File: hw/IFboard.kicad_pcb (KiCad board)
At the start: 2 copper layers, 85 x 65.1 mm, 79 parts, among them J1 USB_C_Receptacle_USB2.0_16P, J2 Conn_01x03_Socket, J3 Conn_ARM_SWD_TagConnect_TC203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, J4 Conn_01x03_Socket, J5 Conn_01x03_Socket, J6 Conn_01x03_Socket, J7 Conn_01x01_MountingPin, SW3 SW_Push, SW4 SW_Push, SW5 SW_Push, SW6 SW_Push, U2 XC6206PxxxMR, U3 TCAN3413DR, U4 ST4E1240DT, U5 MAX232ESE+T, U6 STM32G0B1CBTx, U7 ER_OLEDM0.91_1x-I2C

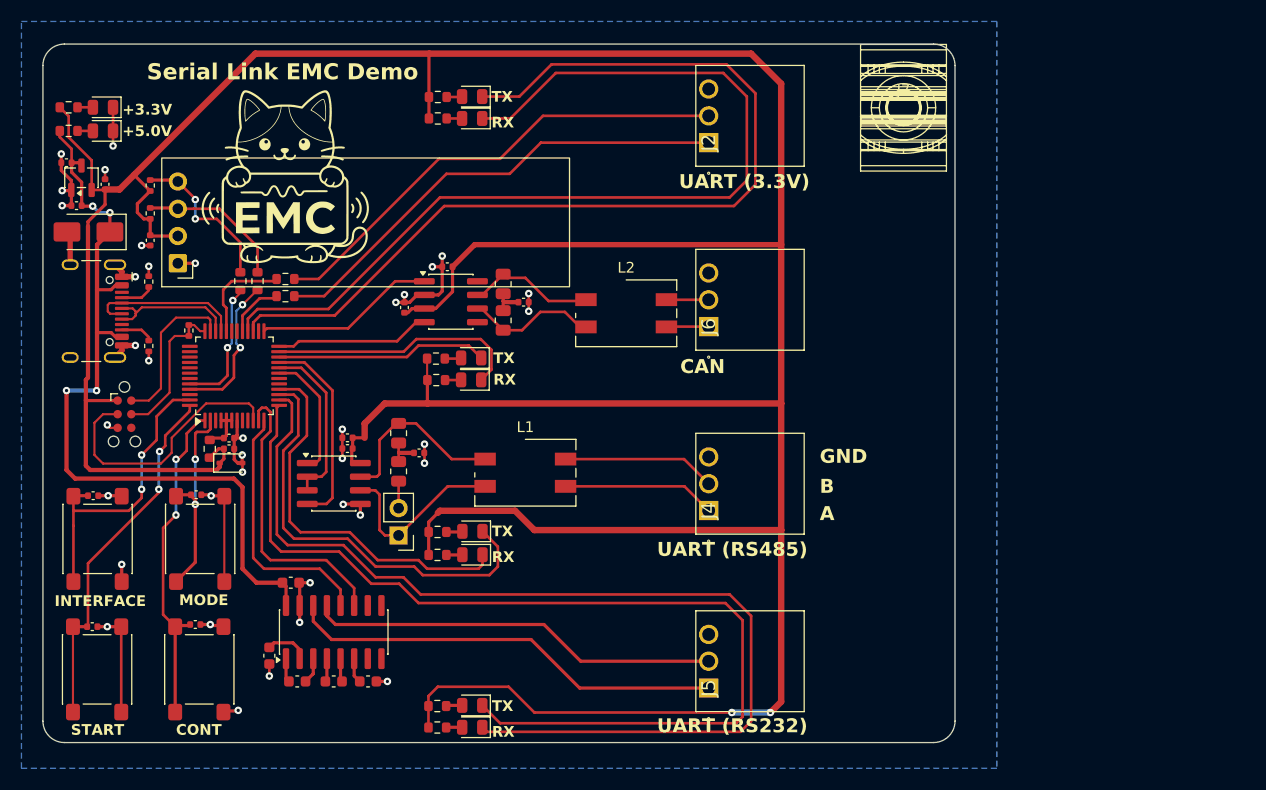
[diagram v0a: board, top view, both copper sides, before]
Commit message: changed position of SMSs and added TVS diodes to RS485 and CAN
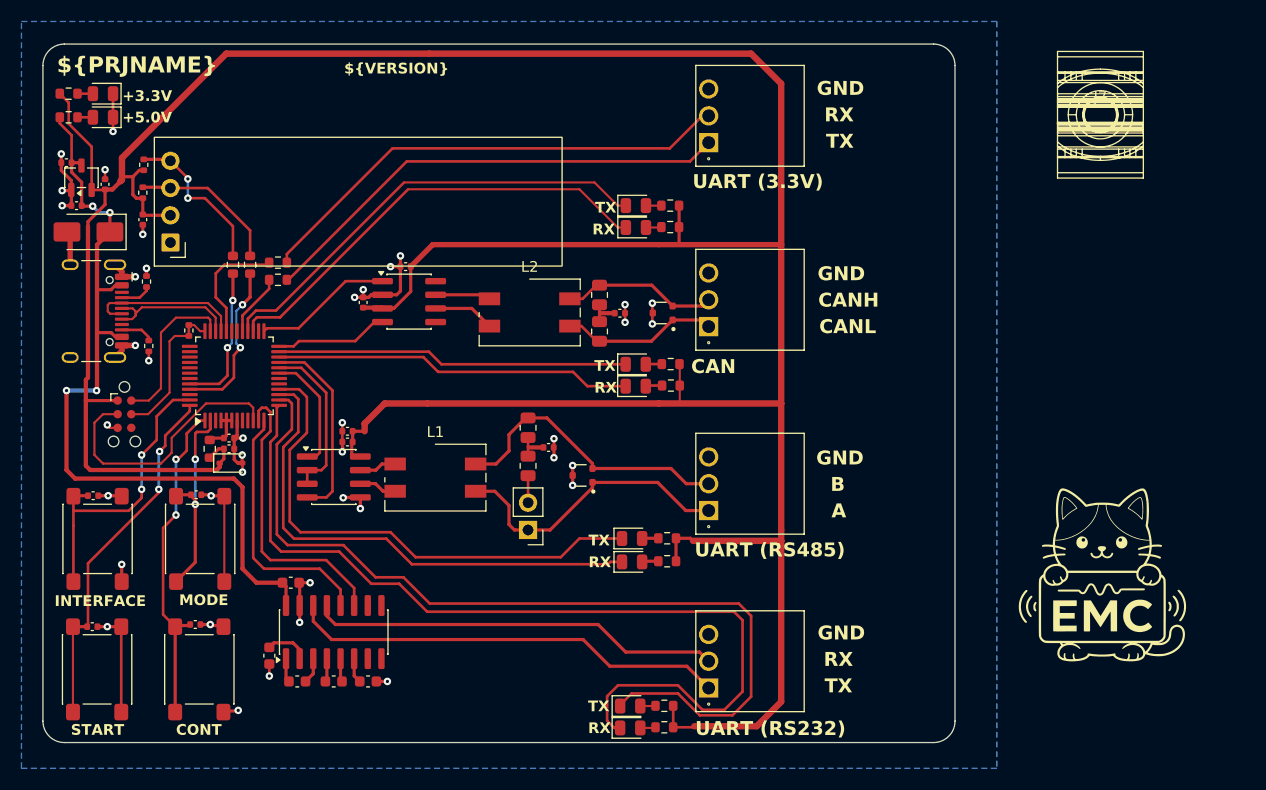
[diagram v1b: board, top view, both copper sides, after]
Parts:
- added D13: PESD2CANFD24V-UX, PZL:TVS_PESD2CANFD24V-UX, F.Cu at (108.7, 75.4)
- added D14: PESD2CANFD24V-UX, PZL:TVS_PESD2CANFD24V-UX, F.Cu at (101.2, 90.5)
- moved G*** 84.7 mm to (149.7, 99.7)
- moved R11 24.8 mm to (109.4, 67.4), turned to 0 degrees
- moved R10 23.1 mm to (109.4, 65.4), turned to 0 degrees
- moved R13 22.0 mm to (109.5, 82.2), turned to 0 degrees
- moved R12 21.9 mm to (109.4, 80.2), turned to 0 degrees
- moved R17 21.6 mm to (109.1, 98.5), turned to 0 degrees
- moved R16 21.5 mm to (109.1, 96.4), turned to 0 degrees
- moved R18 21.3 mm to (108.8, 112.0), turned to 0 degrees
- moved R19 21.2 mm to (108.8, 114.0), turned to 0 degrees
- moved D5 19.5 mm to (106.2, 67.4), turned to 0 degrees
- moved J7 18.4 mm to (149.5, 56.9)
- moved D4 17.3 mm to (106.2, 65.4), turned to 0 degrees
- moved D8 15.6 mm to (106.2, 82.2), turned to 0 degrees
- moved D6 15.4 mm to (106.2, 80.2), turned to 0 degrees
- moved D10 15.1 mm to (105.8, 98.6), turned to 0 degrees
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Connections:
- JP1 pad 1: Net-(JP1-A) -> Net-(J4-Pin_1)
- L1 pad 2: Net-(JP1-A) -> Net-(U4-A)
- R14 pad 1: Net-(U3-CANH) -> Net-(J6-Pin_2)
- R15 pad 2: Net-(U3-CANL) -> Net-(J6-Pin_1)
- R25 pad 2: Net-(U4-B) -> Net-(J4-Pin_2)
- U4 pad 6: Net-(JP1-A) -> Net-(U4-A)
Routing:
- net +3.3V: track 362.7 -> 315.0 mm, vias 2 -> 0
- net /USART1_RX_LED: track 89.3 -> 42.2 mm
- net /USART1_TX_LED: track 88.1 -> 42.5 mm
- net Net-(JP1-A): track 17.2 -> 0.00 mm
- net /CAN_RX_LED: track 19.8 -> 33.4 mm
- net /USART4_TX_LED: track 96.9 -> 83.3 mm
- net Net-(U4-B): track 16.9 -> 3.48 mm
- net Net-(J4-Pin_1): track 14.3 -> 27.5 mm
- net Net-(J4-Pin_2): track 14.3 -> 27.2 mm
- net /USART3_TX_LED: track 36.0 -> 48.0 mm
- net Net-(J6-Pin_2): track 3.94 -> 14.6 mm
- net Net-(J6-Pin_1): track 3.95 -> 14.6 mm
- net /USART4_RX_LED: track 94.2 -> 85.2 mm
- net /CAN_TX_LED: track 23.9 -> 32.8 mm
- net Net-(U3-CANH): track 12.0 -> 5.17 mm
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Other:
- board text added: "${PRJNAME}"
- board text added: "${VERSION}"
- board text added: "CANH"
- board text added: "CANL"
- board text removed: "Serial Link EMC Demo"

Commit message: wip:testpoints
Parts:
- added TP1: TestPoint, PZL:TestPoint_Keystone_5019_Miniature, F.Cu at (101.9, 70.6)
- added TP2: TestPoint, TestPoint:TestPoint_Keystone_5005-5009_Compact, F.Cu at (106.2, 72.8)
- added TP3: TestPoint, TestPoint:TestPoint_Keystone_5005-5009_Compact, F.Cu at (106.2, 78.0)
- added TP4: TestPoint, TestPoint:TestPoint_Keystone_5005-5009_Compact, F.Cu at (105.7, 87.6)
- added TP5: TestPoint, TestPoint:TestPoint_Keystone_5005-5009_Compact, F.Cu at (105.7, 93.1)
- moved D14 7.75 mm to (109.0, 90.5)
- moved D6 0.76 mm to (106.2, 80.9)
- moved D8 0.76 mm to (106.2, 83.0)
- moved R12 0.76 mm to (109.4, 80.9)
- moved R13 0.76 mm to (109.5, 82.9)
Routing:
- net +3.3V: track 315.0 -> 315.8 mm

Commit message: wip:testpoints
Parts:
- added JP2: Jumper_2_Open, Connector_PinHeader_2.54mm:PinHeader_1x02_P2.54mm_Vertical, F.Cu at (103.2, 68.9)
- added R26: 1k, Resistor_SMD:R_0603_1608Metric, F.Cu at (86.7, 77.8)
- added R27: 1k, Resistor_SMD:R_0603_1608Metric, F.Cu at (83.7, 77.8)
- added TP6: TestPoint, TestPoint:TestPoint_Keystone_5005-5009_Compact, F.Cu at (107.2, 58.3)
- added TP7: TestPoint, TestPoint:TestPoint_Keystone_5005-5009_Compact, F.Cu at (107.1, 53.4)
- added TP8: TestPoint, TestPoint:TestPoint_Keystone_5005-5009_Compact, F.Cu at (107.2, 108.3)
- added TP9: TestPoint, TestPoint:TestPoint_Keystone_5005-5009_Compact, F.Cu at (107.2, 104.0)
- U7: footprint Display:ER_OLEDM0.91_1x-I2C -> PZL:ER_OLEDM0.91_1x-I2C
- moved TP1 18.6 mm to (91.4, 55.2), turned to -90 degrees
- moved D5 4.10 mm to (105.9, 63.3)
- moved D4 4.10 mm to (105.9, 61.3)
- moved R10 4.10 mm to (109.1, 61.3)
- moved R11 4.10 mm to (109.1, 63.3)
- moved TP5 1.81 mm to (107.2, 94.0), turned to 90 degrees
- moved TP2 1.63 mm to (107.2, 71.5)
- moved TP4 1.61 mm to (107.2, 87.1)
- moved C20 1.61 mm to (104.2, 76.9)
- moved R15 1.61 mm to (102.3, 78.6)
- moved R14 1.44 mm to (102.2, 75.0)
- moved D10 1.27 mm to (105.8, 99.9)
- moved D9 1.27 mm to (105.8, 97.7)
- moved R16 1.27 mm to (109.1, 97.7)
- moved R17 1.27 mm to (109.1, 99.8)
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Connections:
- R14 pad 1: Net-(J6-Pin_2) -> Net-(JP2-B)
- U3 pad 5: unconnected-(U3-SHDN-Pad5) -> Net-(U3-SHDN)
- U3 pad 8: unconnected-(U3-S-Pad8) -> Net-(U3-S)
- U6 pad 26: unconnected-(U6-PB14-Pad26) -> /TODO_EN_CAN_TERM
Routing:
- net Net-(U3-S): track 0.00 -> 7.36 mm
- net Net-(J2-Pin_2): track 45.4 -> 49.7 mm
- net GND: track 87.7 -> 91.6 mm, vias 40 -> 43
- net Net-(J6-Pin_2): track 14.6 -> 18.4 mm
- net Net-(J2-Pin_1): track 44.5 -> 47.7 mm
- net Net-(JP2-B): track 0.00 -> 3.06 mm
- net Net-(J6-Pin_1): track 14.6 -> 17.5 mm
- net Net-(J4-Pin_1): track 27.0 -> 29.2 mm
- net Net-(J4-Pin_2): track 26.9 -> 29.0 mm
- net Net-(U3-SHDN): track 0.00 -> 1.61 mm
- net /USART1_RX_LED: track 42.2 -> 40.7 mm
- net Net-(U6-PB6): track 15.2 -> 13.9 mm
- net Net-(U6-PB5): track 13.5 -> 12.3 mm
- net /USART1_RX: track 11.4 -> 10.1 mm
- net /SCL: track 14.0 -> 15.3 mm
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
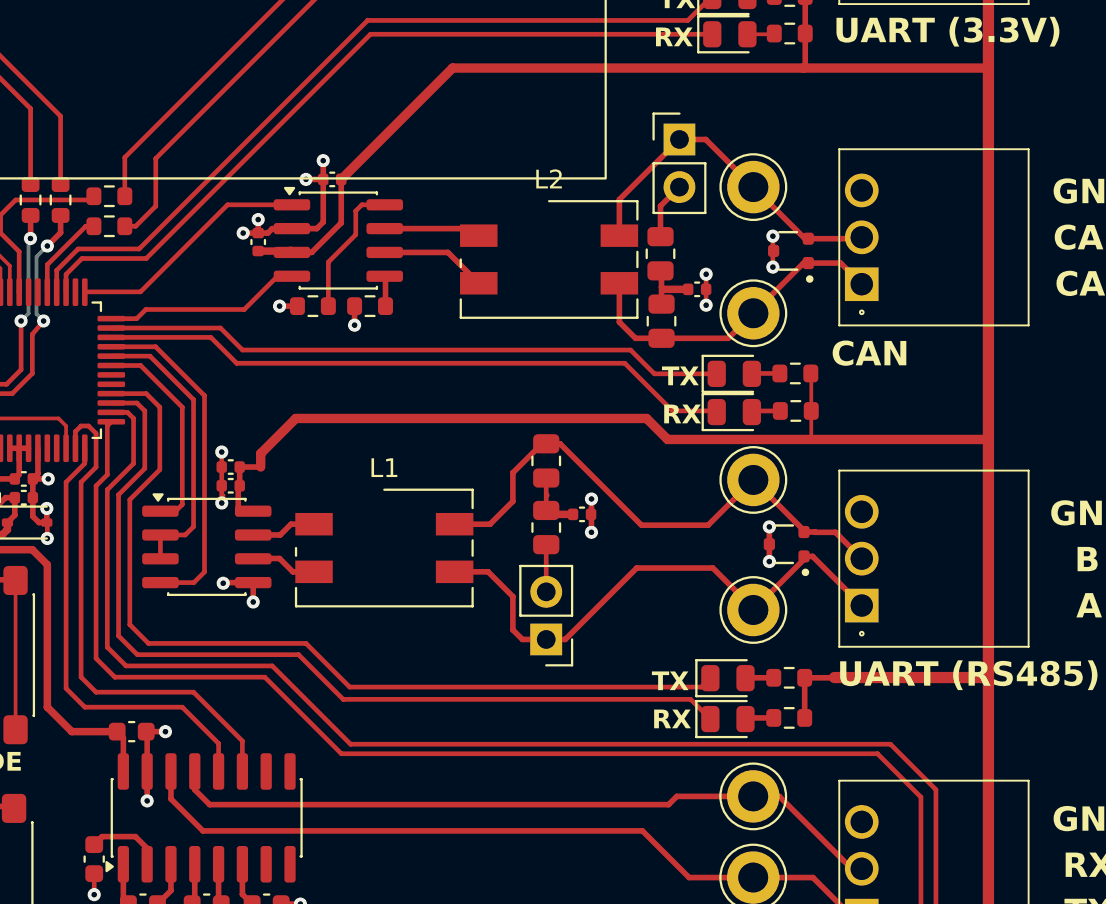
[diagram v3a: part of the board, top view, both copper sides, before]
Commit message: added jumper to add/remove split-termination capacitors
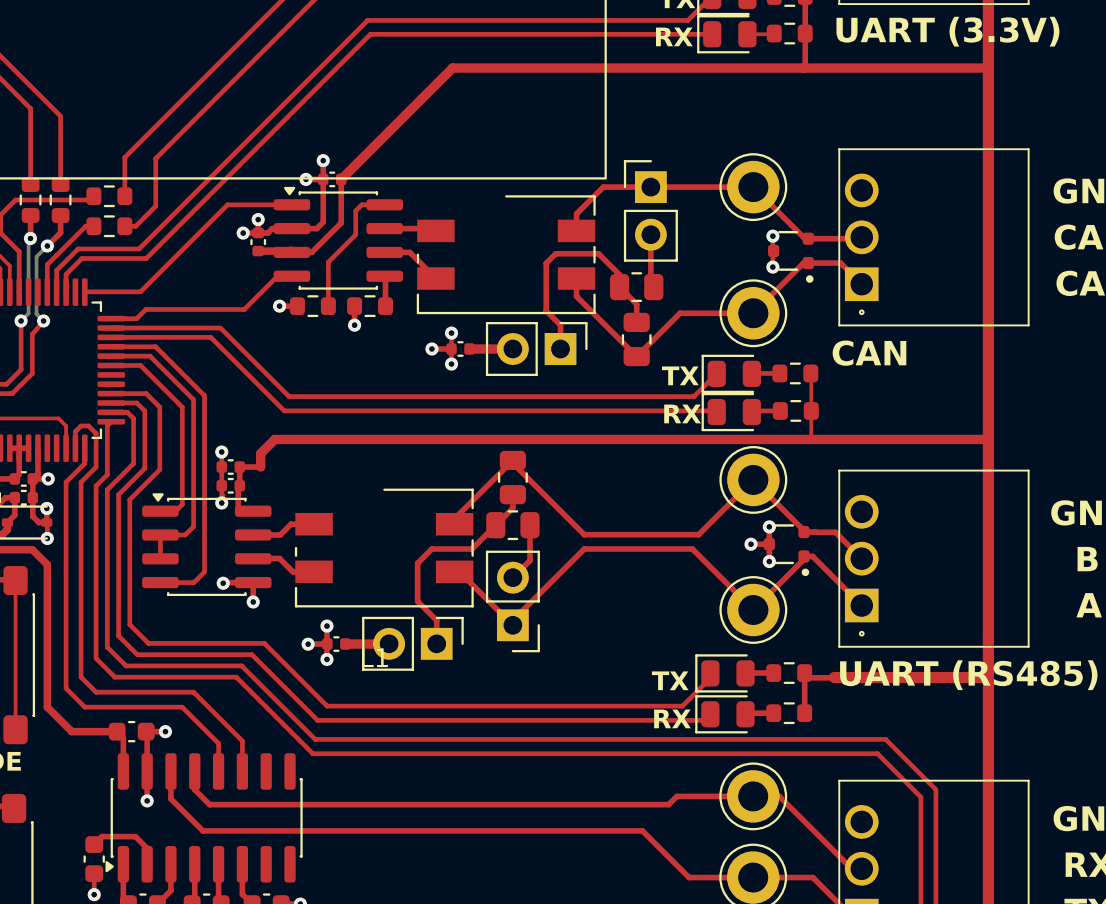
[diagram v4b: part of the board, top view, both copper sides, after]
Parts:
- added JP3: Jumper_2_Open, Connector_PinHeader_2.54mm:PinHeader_1x02_P2.54mm_Vertical, F.Cu at (90.3, 95.8)
- added JP4: Jumper_2_Open, Connector_PinHeader_2.54mm:PinHeader_1x02_P2.54mm_Vertical, F.Cu at (96.9, 80.1)
- C24: value 220p -> 10nF
- moved C24 14.8 mm to (84.9, 95.9), turned to 0 degrees
- moved C20 13.0 mm to (91.6, 80.1), turned to 0 degrees
- moved JP2 2.96 mm to (101.7, 71.5)
- moved L2 2.30 mm to (94.0, 75.1)
- moved R14 2.18 mm to (101.0, 76.8), turned to 180 degrees
- moved R25 1.99 mm to (94.4, 87.0)
- moved JP1 1.93 mm to (94.4, 94.9)
- moved R24 1.78 mm to (94.4, 89.5), turned to 180 degrees
- moved R15 1.64 mm to (101.0, 79.6)
- moved D10 0.25 mm to (105.8, 99.6)
- moved R16 0.25 mm to (109.1, 97.4)
- moved R17 0.25 mm to (109.1, 99.5)
- moved D9 0.25 mm to (105.8, 97.4)
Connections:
- C20 pad 2: Net-(C20-Pad2) -> Net-(JP4-B)
- C24 pad 2: Net-(C24-Pad2) -> Net-(JP3-B)
- R14 pad 2: Net-(C20-Pad2) -> Net-(JP4-A)
- R15 pad 1: Net-(C20-Pad2) -> Net-(JP4-A)
- R24 pad 2: Net-(C24-Pad2) -> Net-(JP3-A)
- R25 pad 1: Net-(C24-Pad2) -> Net-(JP3-A)
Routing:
- net Net-(JP4-A): track 0.00 -> 12.4 mm
- net Net-(JP3-A): track 0.00 -> 11.7 mm
- net Net-(C20-Pad2): track 3.26 -> 0.00 mm
- net Net-(C24-Pad2): track 3.19 -> 0.00 mm
- net GND: track 91.6 -> 94.6 mm, vias 43 -> 46
- net Net-(J6-Pin_1): track 17.5 -> 20.0 mm
- net Net-(U3-CANH): track 5.17 -> 2.78 mm
- net Net-(U3-CANL): track 5.70 -> 3.31 mm
- net Net-(JP3-B): track 0.00 -> 2.34 mm
- net Net-(JP4-B): track 0.00 -> 2.31 mm
- net /CAN_TX_LED: track 33.3 -> 34.3 mm
- net Net-(J4-Pin_2): track 29.0 -> 28.0 mm
- net +3.3V: track 316.7 -> 315.8 mm
- net /USART3_TX_LED: track 47.7 -> 48.5 mm
- net Net-(JP1-B): track 2.52 -> 3.18 mm
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
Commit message: train session
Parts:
- removed the G*** at (149.7, 99.7)
- added J10: Conn_01x01_MountingPin, Connector_PinHeader_1.00mm:PinHeader_1x01_P1.00mm_Vertical, F.Cu at (146.9, 107.8)
- added J8: Conn_01x01_MountingPin, Connector_PinHeader_1.00mm:PinHeader_1x01_P1.00mm_Vertical, F.Cu at (146.8, 74.2)
- added J9: Conn_01x01_MountingPin, Connector_PinHeader_1.00mm:PinHeader_1x01_P1.00mm_Vertical, F.Cu at (146.9, 91.4)
- added TP10: TestPoint, PZL:TestPoint_Keystone_5019_Miniature, F.Cu at (91.4, 85.3)
- added TP11: TestPoint, PZL:TestPoint_Keystone_5019_Miniature, F.Cu at (91.4, 109.4)
- R14, R15, R24, R25: value 56 -> 68
- moved J7 2.71 mm to (146.8, 57.3)
- moved SW6 0.08 mm to (65.6, 108.6)
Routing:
- net GND: track 94.6 -> 115.2 mm, vias 46 -> 55
- net +3.3V: track 315.8 -> 318.9 mm
- net /CAN_TX_LED: track 34.3 -> 33.5 mm
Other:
- board size 85 x 65.1 mm -> 105 x 65.1 mm
- board text added: "CAN_C"
- board text added: "CAN_R"
- board text added: "RS485_C"
- board text added: "RS485_R"
- board text added: "U4_RX"
- board text added: "U4_TX"

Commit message: cleanup
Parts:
- J10, J7, J8, J9: value Conn_01x01_MountingPin -> IcoTec_36650.2; footprint Connector_PinHeader_1.00mm:PinHeader_1x01_P1.00mm_Vertical -> PZ:icotek 36650.2 PCB-4-V-6,8SKL 3-6
- U2: value XC6206PxxxMR -> XC6206P332MR-G

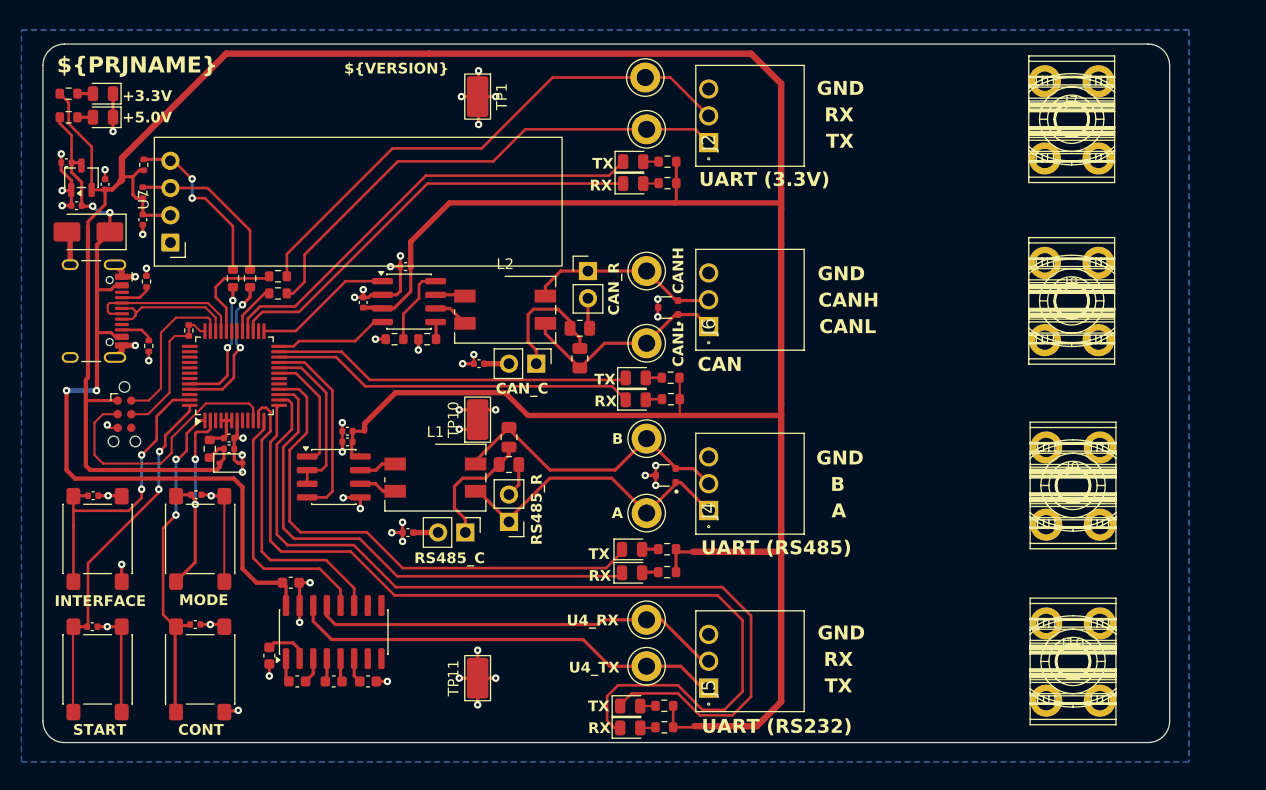
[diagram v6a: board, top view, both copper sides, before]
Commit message: modified connectors to vertical
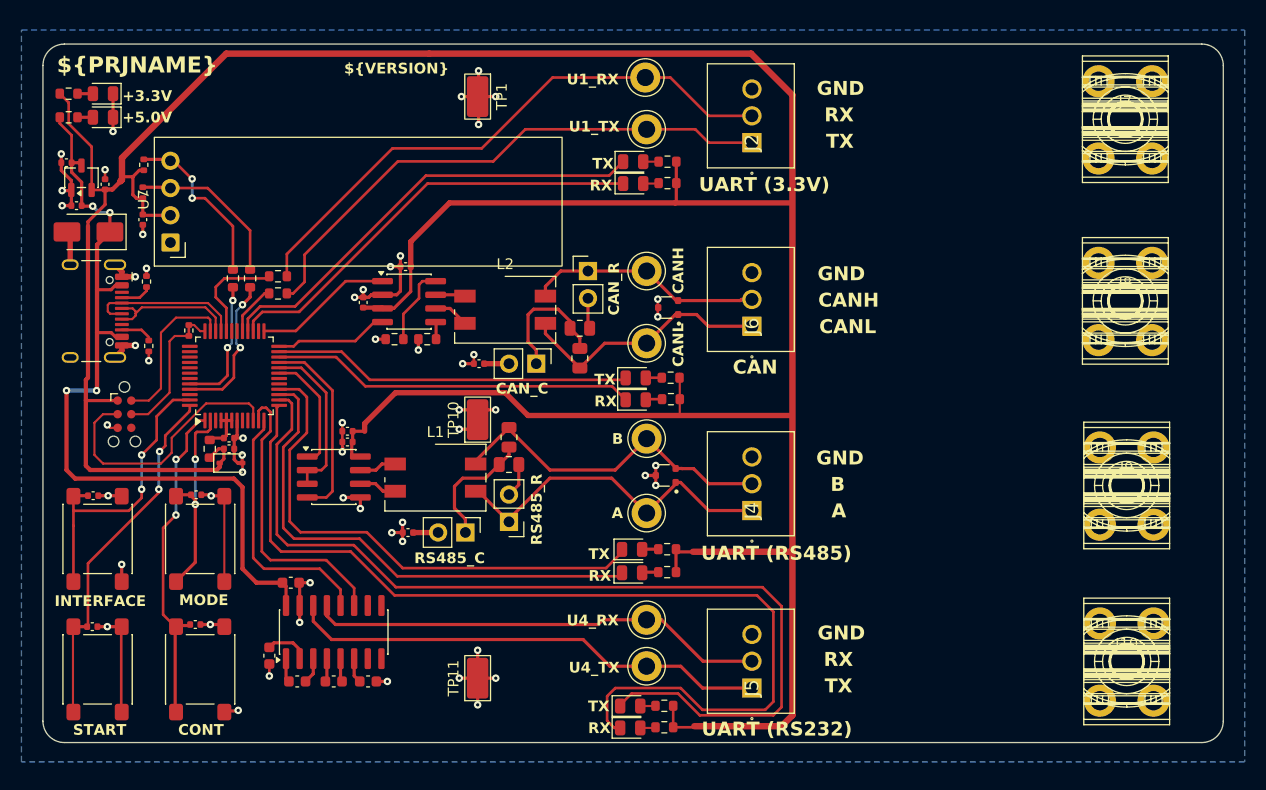
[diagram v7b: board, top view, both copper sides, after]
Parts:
- J2, J4, J5, J6: value Conn_01x03_Socket -> Phoenix_1881561; footprint PZL:1881451 -> PZ:1881561
- TP2, TP3, TP4, TP5, TP6, TP7, TP8, TP9: footprint TestPoint:TestPoint_Keystone_5005-5009_Compact -> PZ:TP_Keystone_5010-5014_Multipurpose
- moved J10 5.00 mm to (151.9, 107.8)
- moved J7 5.00 mm to (151.8, 57.3)
- moved J8 5.00 mm to (151.8, 74.2)
- moved J9 5.00 mm to (151.9, 91.4)
- moved J6 4.03 mm to (117.0, 76.6)
- moved J2 4.03 mm to (117.0, 59.5)
- moved J4 4.03 mm to (117.0, 93.8)
- moved J5 4.03 mm to (117.0, 110.3)
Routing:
- net /USART4_TX_LED: track 83.3 -> 90.0 mm
- net /USART4_RX_LED: track 85.2 -> 91.7 mm
- net +3.3V: track 318.9 -> 324.3 mm
- net /USART4_RX_MAX: track 38.7 -> 42.7 mm
- net Net-(J4-Pin_2): track 28.0 -> 32.1 mm
- net Net-(J4-Pin_1): track 28.7 -> 32.7 mm
- net Net-(J2-Pin_2): track 49.7 -> 53.7 mm
- net Net-(J2-Pin_1): track 47.7 -> 51.7 mm
- net /USART4_TX_MAX: track 40.9 -> 44.9 mm
- net Net-(J6-Pin_2): track 17.9 -> 21.9 mm
- net Net-(J6-Pin_1): track 20.0 -> 24.0 mm
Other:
- board size 105 x 65.1 mm -> 110 x 65.1 mm
- board text added: "U1_RX"
- board text added: "U1_TX"
